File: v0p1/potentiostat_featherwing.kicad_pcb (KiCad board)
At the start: 2 copper layers, 16 parts, among them J1 Screw_Terminal_01x03, P1 pin_array_3x1, U1 feather_wing, U2 LMP7721, U3 LMP7721, U4 LMP7721, U5 LMP7721

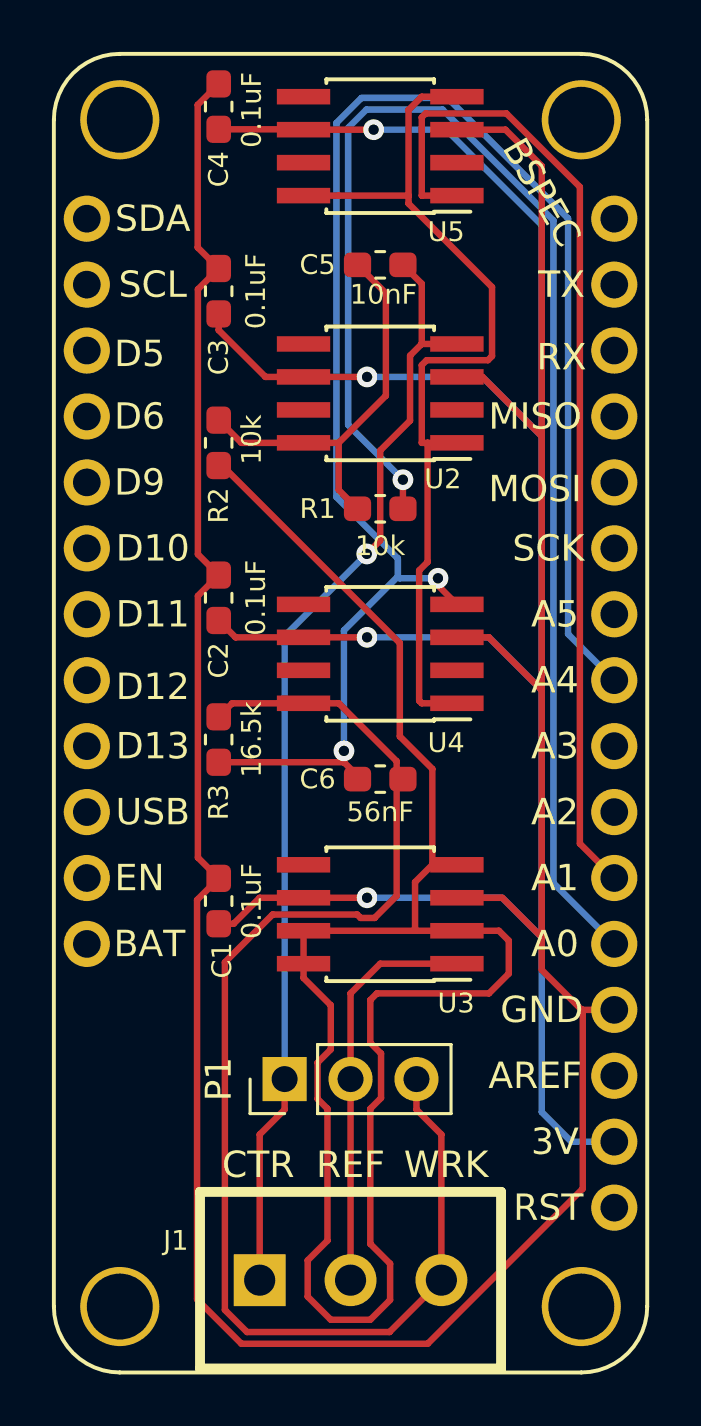
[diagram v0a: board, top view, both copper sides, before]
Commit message: Added new v0.2 version of the featherwing design.
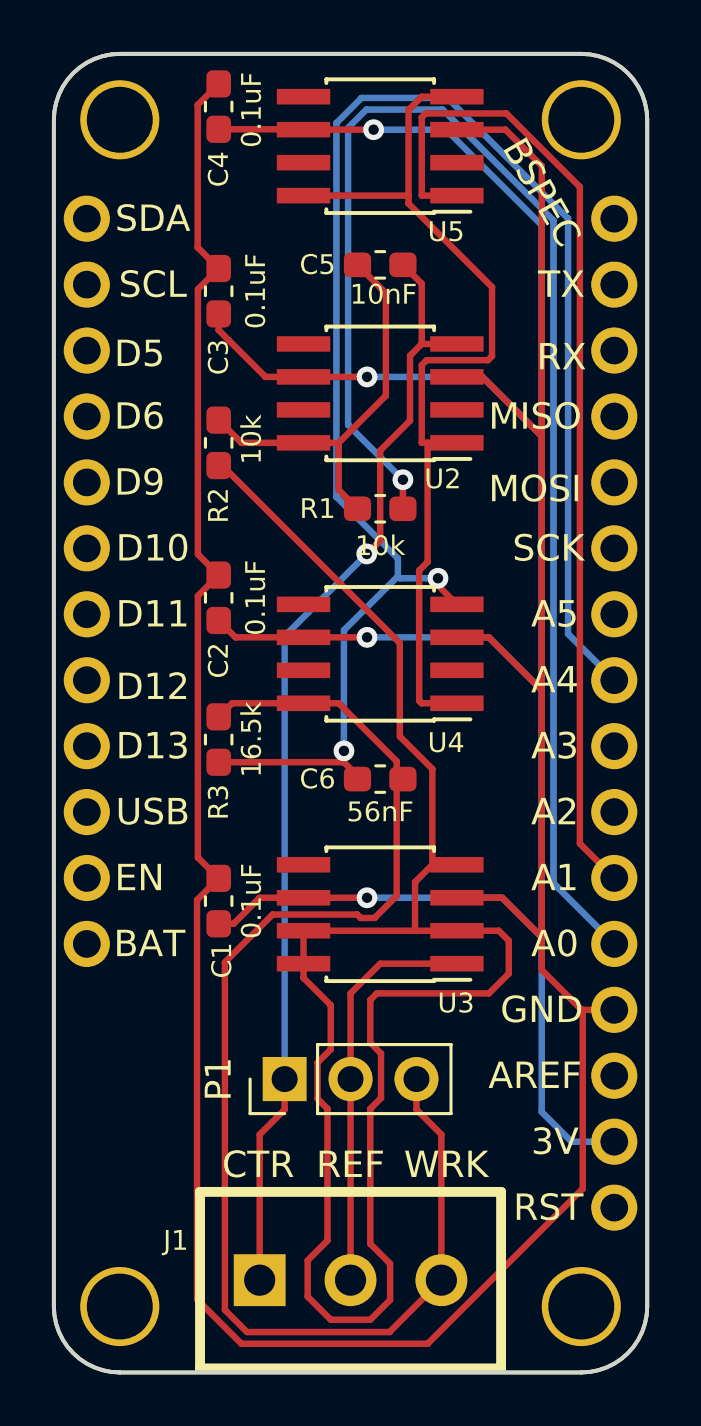
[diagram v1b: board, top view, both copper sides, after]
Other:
- board outline added: 22.9 x 50.8 mm
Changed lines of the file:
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@@
   (general
     (thickness 1.6)
-    (drawings 4)
+    (drawings 14)
     (tracks 200)
     (zones 0)
@@
     )
   )
+  (dimension 22.86 (width 0.3) (layer Dwgs.User)
+    (gr_text "0.9000 in" (at 50.8 84.65) (layer Dwgs.User)
+      (effects (font (size 1.5 1.5) (thickness 0.3)))
+    )
+    (feature1 (pts (xy 62.23 73.66) (xy 62.23 83.136421)))
+    (feature2 (pts (xy 39.37 73.66) (xy 39.37 83.136421)))
+    (crossbar (pts (xy 39.37 82.55) (xy 62.23 82.55)))
+    (arrow1a (pts (xy 62.23 82.55) (xy 61.103496 83.136421)))
+    (arrow1b (pts (xy 62.23 82.55) (xy 61.103496 81.963579)))
+    (arrow2a (pts (xy 39.37 82.55) (xy 40.496504 83.136421)))
+    (arrow2b (pts (xy 39.37 82.55) (xy 40.496504 81.963579)))
+  )
+  (dimension 50.8 (width 0.3) (layer Dwgs.User)
+    (gr_text "2.0000 in" (at 68.648 50.8 270) (layer Dwgs.User)
+      (effects (font (size 1.5 1.5) (thickness 0.3)))
+    )
+    (feature1 (pts (xy 59.69 76.2) (xy 67.134421 76.2)))
+    (feature2 (pts (xy 59.69 25.4) (xy 67.134421 25.4)))
+    (crossbar (pts (xy 66.548 25.4) (xy 66.548 76.2)))
+    (arrow1a (pts (xy 66.548 76.2) (xy 65.961579 75.073496)))
+    (arrow1b (pts (xy 66.548 76.2) (xy 67.134421 75.073496)))
+    (arrow2a (pts (xy 66.548 25.4) (xy 65.961579 26.526504)))
+    (arrow2b (pts (xy 66.548 25.4) (xy 67.134421 26.526504)))
+  )
+  (gr_line (start 39.37 73.66) (end 39.37 27.94) (layer Edge.Cuts) (width 0.15))
+  (gr_line (start 59.69 76.2) (end 41.91 76.2) (layer Edge.Cuts) (width 0.15))
+  (gr_line (start 62.23 27.94) (end 62.23 73.66) (layer Edge.Cuts) (width 0.15))
+  (gr_arc (start 59.69 27.94) (end 62.23 27.94) (angle -90) (layer Edge.Cuts) (width 0.15))
+  (gr_line (start 41.91 25.4) (end 59.69 25.4) (layer Edge.Cuts) (width 0.15))
+  (gr_arc (start 59.69 73.66) (end 59.69 76.2) (angle -90) (layer Edge.Cuts) (width 0.15))
+  (gr_arc (start 41.91 73.66) (end 39.37 73.66) (angle -90) (layer Edge.Cuts) (width 0.15))
+  (gr_arc (start 41.91 27.94) (end 41.91 25.4) (angle -90) (layer Edge.Cuts) (width 0.15))
   (gr_text "Potentiostat Featherwing v0.1" (at 50.8 46.863 90) (layer B.SilkS)
     (effects (font (size 1.016 1.016) (thickness 0.2032)) (justify mirror))
